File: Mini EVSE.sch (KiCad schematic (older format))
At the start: 30 parts, among them IC1 G3MC-201PL DC5, IC2 IRM-03-5, IC3 ATTINY84-20PU, IC4 RD-0512D, IC5 SI8261BAC-C-IP, J1 RE OUT, J2 AC IN, J3 TX, J4 ICP, J5 SWITCH, J6 PILOTS, X1 15.36MHz

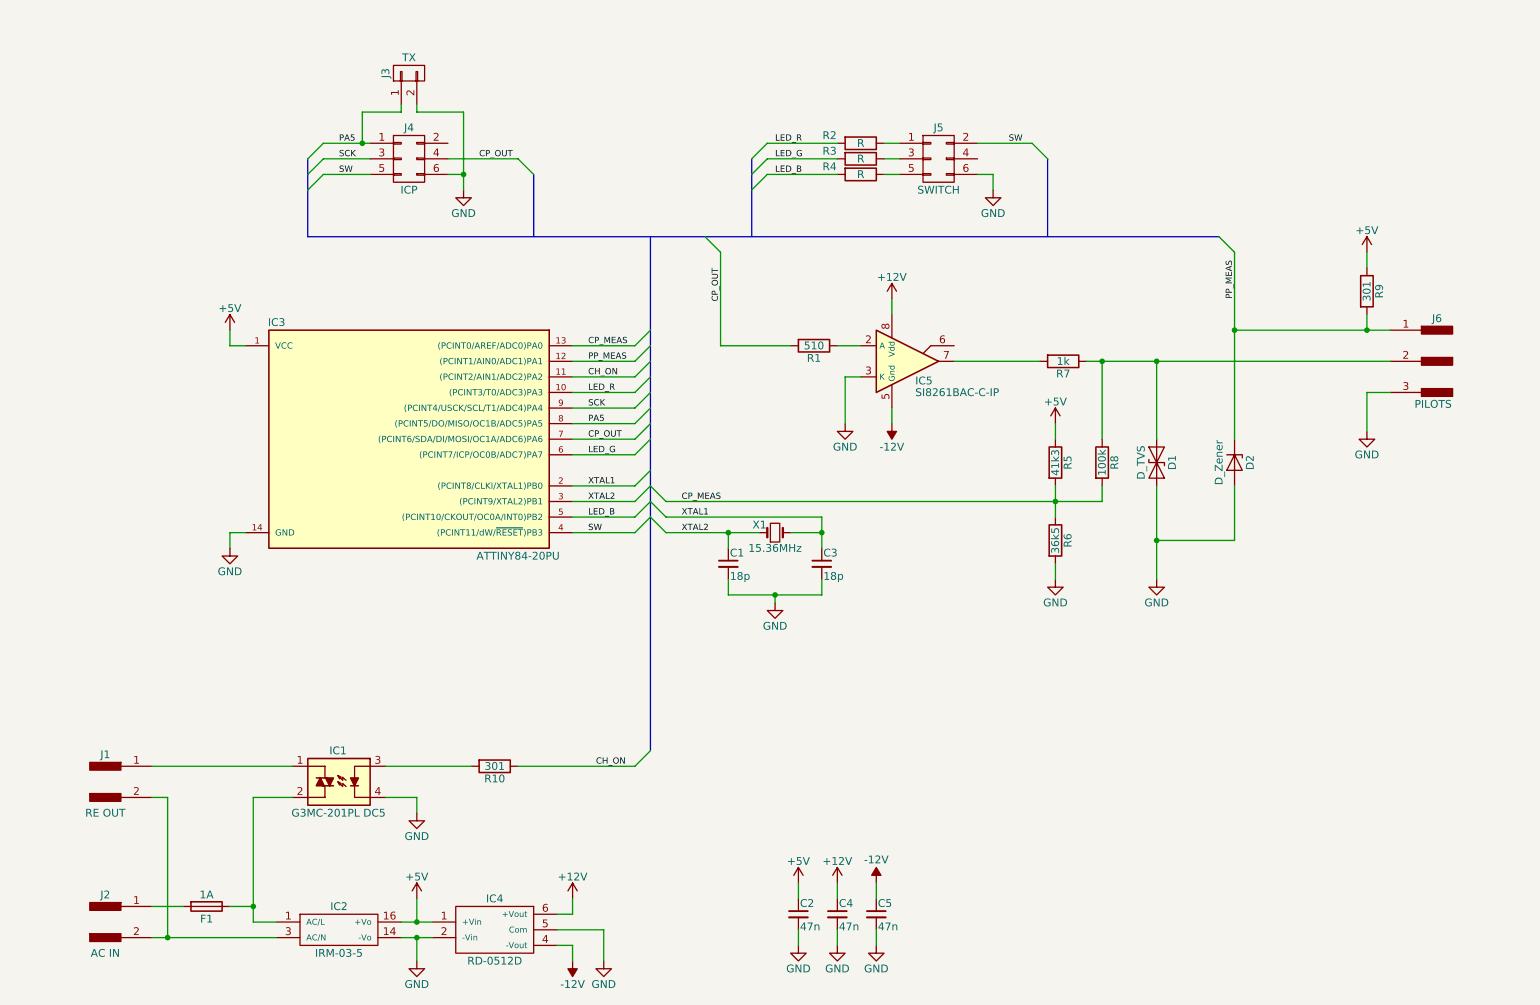
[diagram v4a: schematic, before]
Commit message: Small schematics changes. Added PCB layout
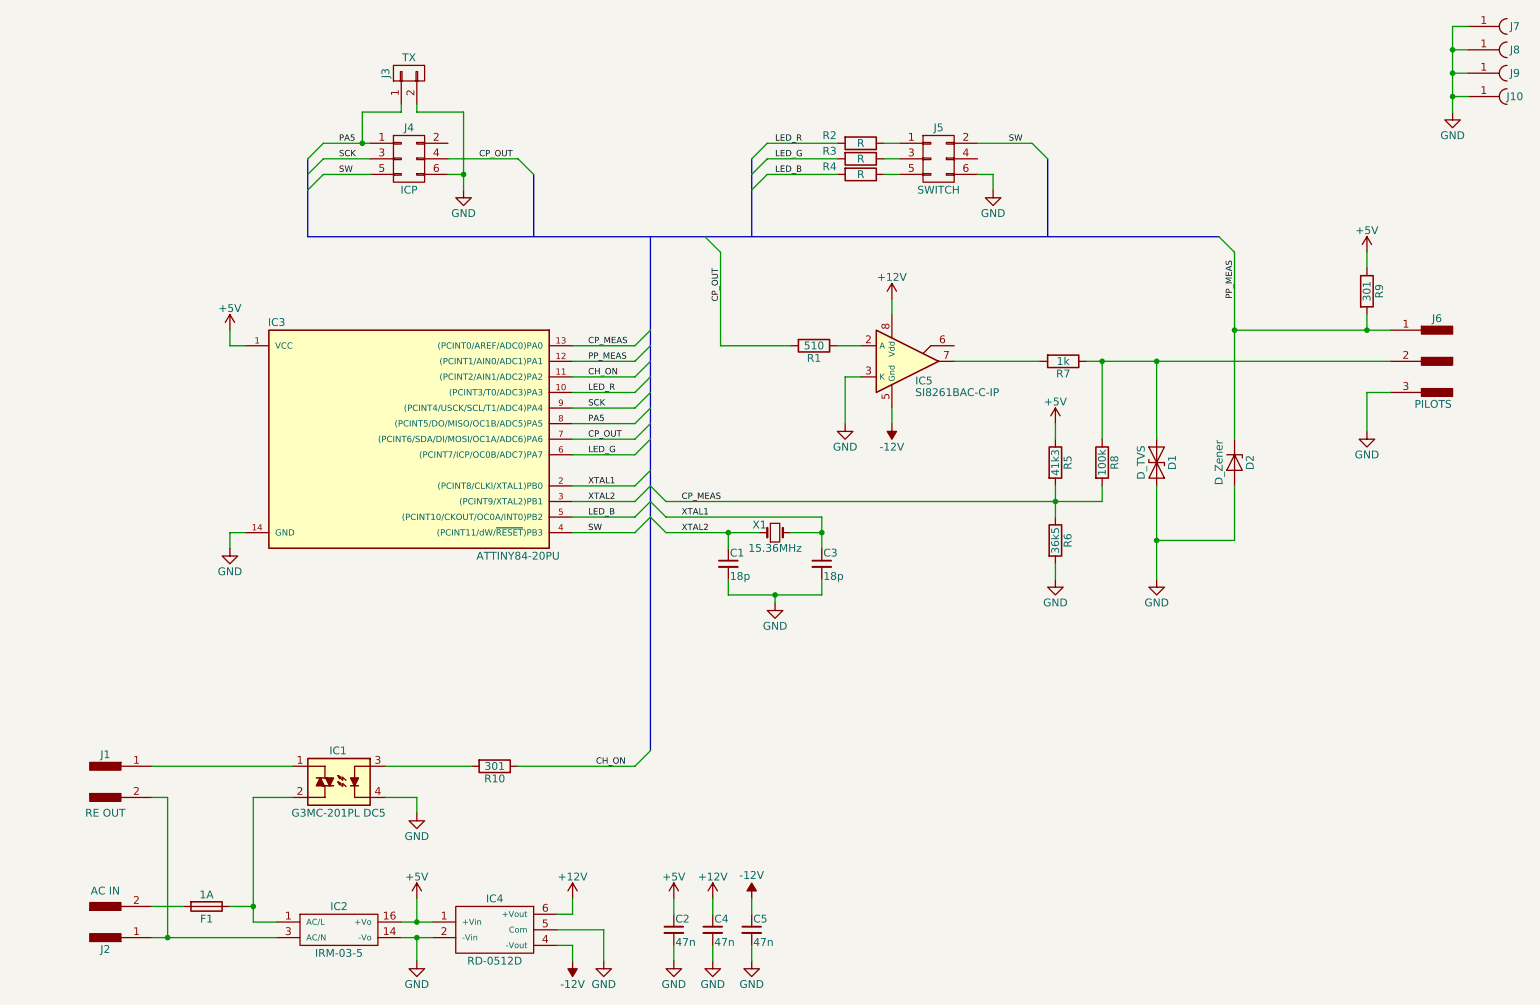
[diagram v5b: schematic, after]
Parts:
- added J10, J7, J8, J9: M, Mounting_Holes:MountingHole_3.2mm_M3_ISO7380_Pad, symbol CONN_01X01_FEMALE
- F1: footprint Miscellaneous:R_Axial_DIN0207_L6.3mm_D2.5mm_P10.16mm_Horizontal -> Fuse_Holders_and_Fuses:Fuseholder_Fuse_TR5_Littlefuse-No560_No460
- J1, J2: footprint Connectors:bornier2 -> Connectors_Terminal_Blocks:TerminalBlock_Pheonix_MKDS1.5-2pol
- J6: footprint Connectors:bornier3 -> Connectors_Terminal_Blocks:TerminalBlock_Pheonix_MKDS1.5-3pol
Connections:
- net GND: now also J10.1, J7.1, J8.1, J9.1
- net at J2.1: now also IC2.3 (AC/N), J1.2; no longer F1.2
- new net: F1.2, J2.2
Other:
- moved on the sheet: C2, C4, C5
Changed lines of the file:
@@
 F 0 "J2" H 1350 6825 50  0000 C CNN
 F 1 "AC IN" H 1350 6450 50  0000 C CNN
-F 2 "Connectors:bornier2" H 1350 6750 50  0001 C CNN
+F 2 "Connectors_Terminal_Blocks:TerminalBlock_Pheonix_MKDS1.5-2pol" H 1350 6750 50  0001 C CNN
 F 3 "" H 1350 6750 50  0001 C CNN
 	1    1350 6650
-	1    0    0    -1
+	1    0    0    1
 $EndComp
 $Comp
@@
 L C_Small C2
 U 1 1 59A6F880
-P 5800 6600
-F 0 "C2" H 5810 6670 50  0000 L CNN
-F 1 "47n" H 5810 6520 50  0000 L CNN
-F 2 "Miscellaneous:C_Disc_D5.1mm_W3.2mm_P5.08mm" H 5800 6600 50  0001 C CNN
-F 3 "" H 5800 6600 50  0001 C CNN
-	1    5800 6600
+P 5000 6700
+F 0 "C2" H 5010 6770 50  0000 L CNN
+F 1 "47n" H 5010 6620 50  0000 L CNN
+F 2 "Miscellaneous:C_Disc_D5.1mm_W3.2mm_P5.08mm" H 5000 6700 50  0001 C CNN
+F 3 "" H 5000 6700 50  0001 C CNN
+	1    5000 6700
 	1    0    0    -1
 $EndComp
@@
 L C_Small C4
 U 1 1 59A6F8CB
-P 6050 6600
-F 0 "C4" H 6060 6670 50  0000 L CNN
-F 1 "47n" H 6060 6520 50  0000 L CNN
-F 2 "Miscellaneous:C_Disc_D5.1mm_W3.2mm_P5.08mm" H 6050 6600 50  0001 C CNN
-F 3 "" H 6050 6600 50  0001 C CNN
-	1    6050 6600
+P 5250 6700
+F 0 "C4" H 5260 6770 50  0000 L CNN
+F 1 "47n" H 5260 6620 50  0000 L CNN
+F 2 "Miscellaneous:C_Disc_D5.1mm_W3.2mm_P5.08mm" H 5250 6700 50  0001 C CNN
+F 3 "" H 5250 6700 50  0001 C CNN
+	1    5250 6700
 	1    0    0    -1
 $EndComp
@@
 L C_Small C5
 U 1 1 59A6F910
-P 6300 6600
-F 0 "C5" H 6310 6670 50  0000 L CNN
-F 1 "47n" H 6310 6520 50  0000 L CNN
-F 2 "Miscellaneous:C_Disc_D5.1mm_W3.2mm_P5.08mm" H 6300 6600 50  0001 C CNN
-F 3 "" H 6300 6600 50  0001 C CNN
-	1    6300 6600
+P 5500 6700
+F 0 "C5" H 5510 6770 50  0000 L CNN
+F 1 "47n" H 5510 6620 50  0000 L CNN
+F 2 "Miscellaneous:C_Disc_D5.1mm_W3.2mm_P5.08mm" H 5500 6700 50  0001 C CNN
+F 3 "" H 5500 6700 50  0001 C CNN
+	1    5500 6700
 	1    0    0    -1
 $EndComp
@@
 L GND #PWR014
 U 1 1 59A6FAEC
-P 5800 6800
-F 0 "#PWR014" H 5800 6550 50  0001 C CNN
-F 1 "GND" H 5800 6650 50  0000 C CNN
-F 2 "" H 5800 6800 50  0001 C CNN
-F 3 "" H 5800 6800 50  0001 C CNN
-	1    5800 6800
+P 5000 6900
+F 0 "#PWR014" H 5000 6650 50  0001 C CNN
+F 1 "GND" H 5000 6750 50  0000 C CNN
+F 2 "" H 5000 6900 50  0001 C CNN
+F 3 "" H 5000 6900 50  0001 C CNN
+	1    5000 6900
 	1    0    0    -1
 $EndComp
@@
 L GND #PWR015
 U 1 1 59A6FB34
-P 6050 6800
-F 0 "#PWR015" H 6050 6550 50  0001 C CNN
-F 1 "GND" H 6050 6650 50  0000 C CNN
-F 2 "" H 6050 6800 50  0001 C CNN
-F 3 "" H 6050 6800 50  0001 C CNN
-	1    6050 6800
+P 5250 6900
+F 0 "#PWR015" H 5250 6650 50  0001 C CNN
+F 1 "GND" H 5250 6750 50  0000 C CNN
+F 2 "" H 5250 6900 50  0001 C CNN
+F 3 "" H 5250 6900 50  0001 C CNN
+	1    5250 6900
 	1    0    0    -1
 $EndComp
@@
 L GND #PWR016
 U 1 1 59A6FB87
-P 6300 6800
-F 0 "#PWR016" H 6300 6550 50  0001 C CNN
-F 1 "GND" H 6300 6650 50  0000 C CNN
-F 2 "" H 6300 6800 50  0001 C CNN
-F 3 "" H 6300 6800 50  0001 C CNN
-	1    6300 6800
+P 5500 6900
+F 0 "#PWR016" H 5500 6650 50  0001 C CNN
+F 1 "GND" H 5500 6750 50  0000 C CNN
+F 2 "" H 5500 6900 50  0001 C CNN
+F 3 "" H 5500 6900 50  0001 C CNN
+	1    5500 6900
 	1    0    0    -1
 $EndComp
@@
 L +5V #PWR017
 U 1 1 59A6FBB8
-P 5800 6400
-F 0 "#PWR017" H 5800 6250 50  0001 C CNN
-F 1 "+5V" H 5800 6540 50  0000 C CNN
-F 2 "" H 5800 6400 50  0001 C CNN
-F 3 "" H 5800 6400 50  0001 C CNN
-	1    5800 6400
+P 5000 6500
+F 0 "#PWR017" H 5000 6350 50  0001 C CNN
+F 1 "+5V" H 5000 6640 50  0000 C CNN
+F 2 "" H 5000 6500 50  0001 C CNN
+F 3 "" H 5000 6500 50  0001 C CNN
+	1    5000 6500
 	1    0    0    -1
 $EndComp
@@
 L +12V #PWR018
 U 1 1 59A6FBF0
-P 6050 6400
-F 0 "#PWR018" H 6050 6250 50  0001 C CNN
-F 1 "+12V" H 6050 6540 50  0000 C CNN
-F 2 "" H 6050 6400 50  0001 C CNN
-F 3 "" H 6050 6400 50  0001 C CNN
-	1    6050 6400
-	1    0    0    -1
-$EndComp
-$Comp
-L -12V #PWR16
+P 5250 6500
+F 0 "#PWR018" H 5250 6350 50  0001 C CNN
+F 1 "+12V" H 5250 6640 50  0000 C CNN
+F 2 "" H 5250 6500 50  0001 C CNN
+F 3 "" H 5250 6500 50  0001 C CNN
+	1    5250 6500
+	1    0    0    -1
+$EndComp
+$Comp
+L -12V #PWR14
 U 1 1 59A6FC28
-P 6300 6400
-F 0 "#PWR16" H 6300 6500 50  0001 C CNN
-F 1 "-12V" H 6300 6550 50  0000 C CNN
-F 2 "" H 6300 6400 50  0001 C CNN
-F 3 "" H 6300 6400 50  0001 C CNN
-	1    6300 6400
+P 5500 6500
+F 0 "#PWR14" H 5500 6600 50  0001 C CNN
+F 1 "-12V" H 5500 6650 50  0000 C CNN
+F 2 "" H 5500 6500 50  0001 C CNN
+F 3 "" H 5500 6500 50  0001 C CNN
+	1    5500 6500
 	1    0    0    -1
 $EndComp
@@
 	4550 6700 4550 6900
 Wire Wire Line
-	5800 6400 5800 6500
-Wire Wire Line
-	5800 6700 5800 6800
-Wire Wire Line
-	6050 6800 6050 6700
-Wire Wire Line
-	6050 6500 6050 6400
-Wire Wire Line
-	6300 6400 6300 6500
-Wire Wire Line
-	6300 6700 6300 6800
+	5000 6500 5000 6600
+Wire Wire Line
+	5000 6800 5000 6900
+Wire Wire Line
+	5250 6900 5250 6800
+Wire Wire Line
+	5250 6600 5250 6500
+Wire Wire Line
+	5500 6500 5500 6600
+Wire Wire Line
+	5500 6800 5500 6900
 $Comp
 L CONN_01X03_MALE J6
@@
 F 0 "J6" H 9900 3325 50  0000 C CNN
 F 1 "PILOTS" H 9925 2775 50  0000 C CNN
-F 2 "Connectors:bornier3" H 9900 3250 50  0001 C CNN
+F 2 "Connectors_Terminal_Blocks:TerminalBlock_Pheonix_MKDS1.5-3pol" H 9900 3250 50  0001 C CNN
 F 3 "" H 9900 3250 50  0001 C CNN
 	1    9900 3050
@@
 F 0 "J1" H 1350 5925 50  0000 C CNN
 F 1 "RE OUT" H 1350 5550 50  0000 C CNN
-F 2 "Connectors:bornier2" H 1350 5850 50  0001 C CNN
+F 2 "Connectors_Terminal_Blocks:TerminalBlock_Pheonix_MKDS1.5-2pol" H 1350 5850 50  0001 C CNN
 F 3 "" H 1350 5850 50  0001 C CNN
 	1    1350 5750
@@
 F 0 "F1" V 2080 6550 50  0000 C CNN
 F 1 "1A" V 1925 6550 50  0000 C CNN
-F 2 "Miscellaneous:R_Axial_DIN0207_L6.3mm_D2.5mm_P10.16mm_Horizontal" V 1930 6550 50  0001 C CNN
+F 2 "Fuse_Holders_and_Fuses:Fuseholder_Fuse_TR5_Littlefuse-No560_No460" V 1930 6550 50  0001 C CNN
 F 3 "" H 2000 6550 50  0001 C CNN
 	1    2000 6550
@@
 Wire Wire Line
 	4750 5650 4000 5650
+$Comp
+L CONN_01X01_FEMALE J7
+U 1 1 59A85185
+P 10200 900
+F 0 "J7" H 10400 900 50  0000 C CNN
+F 1 "M" H 10200 800 50  0001 C CNN
+F 2 "Mounting_Holes:MountingHole_3.2mm_M3_ISO7380_Pad" H 10200 900 50  0001 C CNN
+F 3 "" H 10200 900 50  0001 C CNN
+	1    10200 900
+	1    0    0    -1
+$EndComp
+$Comp
+L CONN_01X01_FEMALE J9
+U 1 1 59A85329
+P 10200 1200
+F 0 "J9" H 10400 1200 50  0000 C CNN
+F 1 "M" H 10200 1100 50  0001 C CNN
+F 2 "Mounting_Holes:MountingHole_3.2mm_M3_ISO7380_Pad" H 10200 1200 50  0001 C CNN
+F 3 "" H 10200 1200 50  0001 C CNN
+	1    10200 1200
+	1    0    0    -1
+$EndComp
+$Comp
+L CONN_01X01_FEMALE J10
+U 1 1 59A853B2
+P 10200 1350
+F 0 "J10" H 10400 1350 50  0000 C CNN
+F 1 "M" H 10200 1250 50  0001 C CNN
+F 2 "Mounting_Holes:MountingHole_3.2mm_M3_ISO7380_Pad" H 10200 1350 50  0001 C CNN
+F 3 "" H 10200 1350 50  0001 C CNN
+	1    10200 1350
+	1    0    0    -1
+$EndComp
+$Comp
+L CONN_01X01_FEMALE J8
+U 1 1 59A852AB
+P 10200 1050
+F 0 "J8" H 10400 1050 50  0000 C CNN
+F 1 "M" H 10200 950 50  0001 C CNN
+F 2 "Mounting_Holes:MountingHole_3.2mm_M3_ISO7380_Pad" H 10200 1050 50  0001 C CNN
+F 3 "" H 10200 1050 50  0001 C CNN
+	1    10200 1050
+	1    0    0    -1
+$EndComp
+$Comp
+L GND #PWR023
+U 1 1 59A857A0
+P 10000 1450
+F 0 "#PWR023" H 10000 1200 50  0001 C CNN
+F 1 "GND" H 10000 1300 50  0000 C CNN
+F 2 "" H 10000 1450 50  0001 C CNN
+F 3 "" H 10000 1450 50  0001 C CNN
+	1    10000 1450
+	1    0    0    -1
+$EndComp
+Wire Wire Line
+	10000 1450 10000 900
+Wire Wire Line
+	10000 900  10100 900
+Wire Wire Line
+	10100 1050 10000 1050
+Connection ~ 10000 1050
+Wire Wire Line
+	10000 1200 10100 1200
+Connection ~ 10000 1200
+Wire Wire Line
+	10000 1350 10100 1350
+Connection ~ 10000 1350
 $EndSCHEMATC

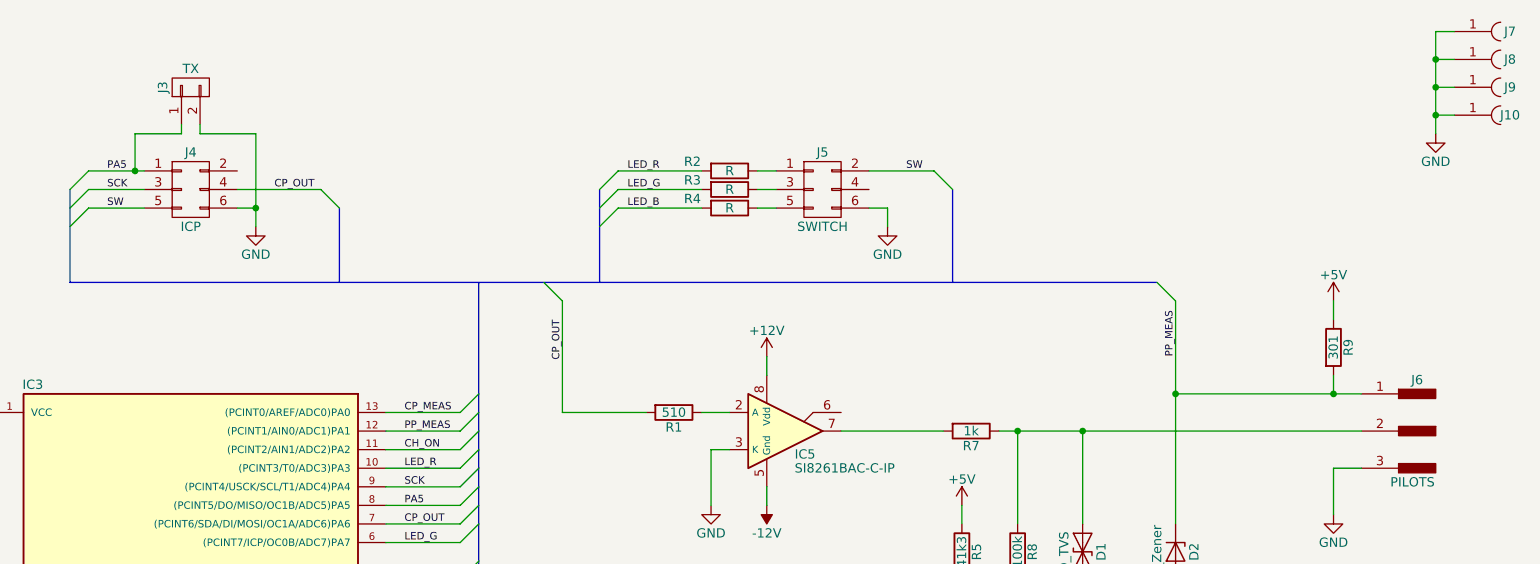
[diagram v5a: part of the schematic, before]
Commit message: Redone PCB design, now 60x70mm. A few schematics changes to make PCB routing easier.
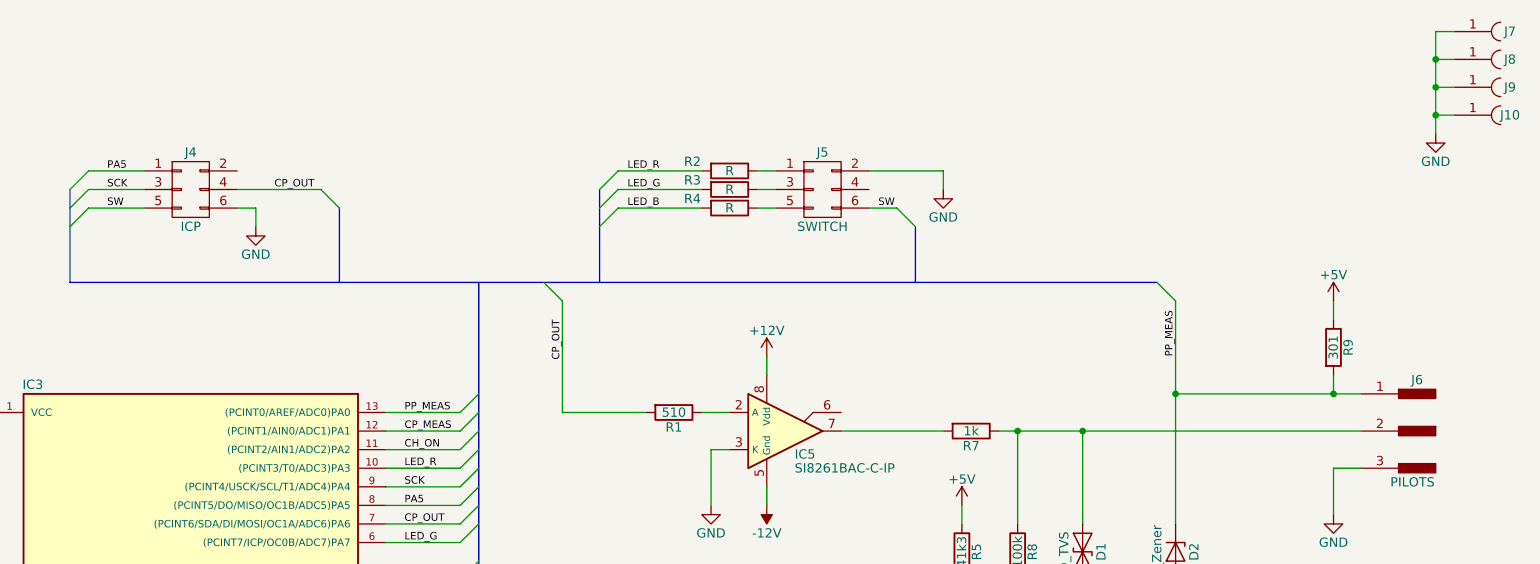
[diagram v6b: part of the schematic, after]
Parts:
- removed J3: TX, Pin_Headers:Pin_Header_Straight_1x02_Pitch2.54mm, symbol CONN_01X02
- D1, D2: footprint Diodes_THT:D_DO-201AD_P12.70mm_Horizontal -> Diodes_THT:D_DO-201_P5.08mm_Vertical_KathodeUp
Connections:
- net CP_MEAS: now also IC3.12 ((PCINT1/AIN0/ADC1)PA1); no longer IC3.13 ((PCINT0/AREF/ADC0)PA0)
- net GND: now also J5.2 (P2); no longer J5.6 (P6)
- net PP_MEAS: now also IC3.13 ((PCINT0/AREF/ADC0)PA0); no longer IC3.12 ((PCINT1/AIN0/ADC1)PA1)
- net SW: now also J5.6 (P6); no longer J5.2 (P2)
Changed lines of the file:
@@
 Entry Wire Line
 	4750 2950 4850 2850
-Text Label 4450 2950 0    40   ~ 0
+Text Label 4450 3050 0    40   ~ 0
 CP_MEAS
 $Comp
@@
 F 0 "D1" H 8100 3800 50  0000 C CNN
 F 1 "D_TVS" H 8100 3600 50  0000 C CNN
-F 2 "Diodes_THT:D_DO-201AD_P12.70mm_Horizontal" H 8100 3700 50  0001 C CNN
+F 2 "Diodes_THT:D_DO-201_P5.08mm_Vertical_KathodeUp" H 8100 3700 50  0001 C CNN
 F 3 "" H 8100 3700 50  0001 C CNN
 	1    8100 3700
@@
 	5750 2950 5300 2950
 Wire Wire Line
-	3650 1450 3650 1950
-Wire Wire Line
 	3650 1850 3550 1850
 Wire Wire Line
@@
 Entry Wire Line
 	4750 3050 4850 2950
-Text Label 4450 3050 0    40   ~ 0
+Text Label 4450 2950 0    40   ~ 0
 PP_MEAS
 $Comp
@@
 F 0 "D2" H 8600 3800 50  0000 C CNN
 F 1 "D_Zener" H 8600 3600 50  0000 C CNN
-F 2 "Diodes_THT:D_DO-201AD_P12.70mm_Horizontal" H 8600 3700 50  0001 C CNN
+F 2 "Diodes_THT:D_DO-201_P5.08mm_Vertical_KathodeUp" H 8600 3700 50  0001 C CNN
 F 3 "" H 8600 3700 50  0001 C CNN
 	1    8600 3700
@@
 L GND #PWR021
 U 1 1 59A71169
-P 7050 1950
-F 0 "#PWR021" H 7050 1700 50  0001 C CNN
-F 1 "GND" H 7050 1800 50  0000 C CNN
-F 2 "" H 7050 1950 50  0001 C CNN
-F 3 "" H 7050 1950 50  0001 C CNN
-	1    7050 1950
-	1    0    0    -1
-$EndComp
-Wire Wire Line
-	6950 1850 7050 1850
-Wire Wire Line
-	7050 1850 7050 1950
+P 7350 1750
+F 0 "#PWR021" H 7350 1500 50  0001 C CNN
+F 1 "GND" H 7350 1600 50  0000 C CNN
+F 2 "" H 7350 1750 50  0001 C CNN
+F 3 "" H 7350 1750 50  0001 C CNN
+	1    7350 1750
+	1    0    0    -1
+$EndComp
 Wire Bus Line
 	5500 1750 5500 2250
@@
 Wire Wire Line
 	6350 1850 6450 1850
-Wire Wire Line
-	6950 1650 7300 1650
-Entry Wire Line
-	7300 1650 7400 1750
-Wire Bus Line
-	7400 1750 7400 2250
-Text Label 7150 1650 0    40   ~ 0
+Entry Wire Line
+	7100 1850 7200 1950
+Text Label 7000 1850 0    40   ~ 0
 SW
 Wire Wire Line
@@
 Entry Wire Line
 	4750 3150 4850 3050
-$Comp
-L CONN_01X02 J3
-U 1 1 59A70B56
-P 3300 1200
-F 0 "J3" H 3300 1350 50  0000 C CNN
-F 1 "TX" V 3400 1200 50  0000 C CNN
-F 2 "Pin_Headers:Pin_Header_Straight_1x02_Pitch2.54mm" H 3300 1200 50  0001 C CNN
-F 3 "" H 3300 1200 50  0001 C CNN
-	1    3300 1200
-	0    -1   -1   0
-$EndComp
 Wire Bus Line
 	4100 1850 4100 2250
-Wire Wire Line
-	3000 1650 3000 1450
-Wire Wire Line
-	3000 1450 3250 1450
-Wire Wire Line
-	3250 1450 3250 1400
-Connection ~ 3000 1650
-Wire Wire Line
-	3650 1450 3350 1450
-Wire Wire Line
-	3350 1450 3350 1400
-Connection ~ 3650 1850
 Text Label 4450 3150 0    40   ~ 0
 CH_ON
@@
 $EndComp
 Wire Wire Line
-	10000 1450 10000 900
+	10000 900  10000 1450
 Wire Wire Line
 	10000 900  10100 900
@@
 	10000 1350 10100 1350
 Connection ~ 10000 1350
+Wire Wire Line
+	3650 1850 3650 1950
+Wire Wire Line
+	6950 1850 7100 1850
+Wire Bus Line
+	7200 1950 7200 2250
+Wire Wire Line
+	6950 1650 7350 1650
+Wire Wire Line
+	7350 1650 7350 1750
 $EndSCHEMATC
